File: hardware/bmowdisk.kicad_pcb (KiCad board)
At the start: 2 copper layers, 100 x 77.7 mm, 41 parts, among them CON1 IDC20, J1 MA06-1NORMAL, J2 MA04-1S, J3 LCD1, J4 M02PTH, U1 LCMXO2-1200HC-TQFP100, U2 SPI-FLASH, U3 MIC5219XX, U4 74X245, U5 74X245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

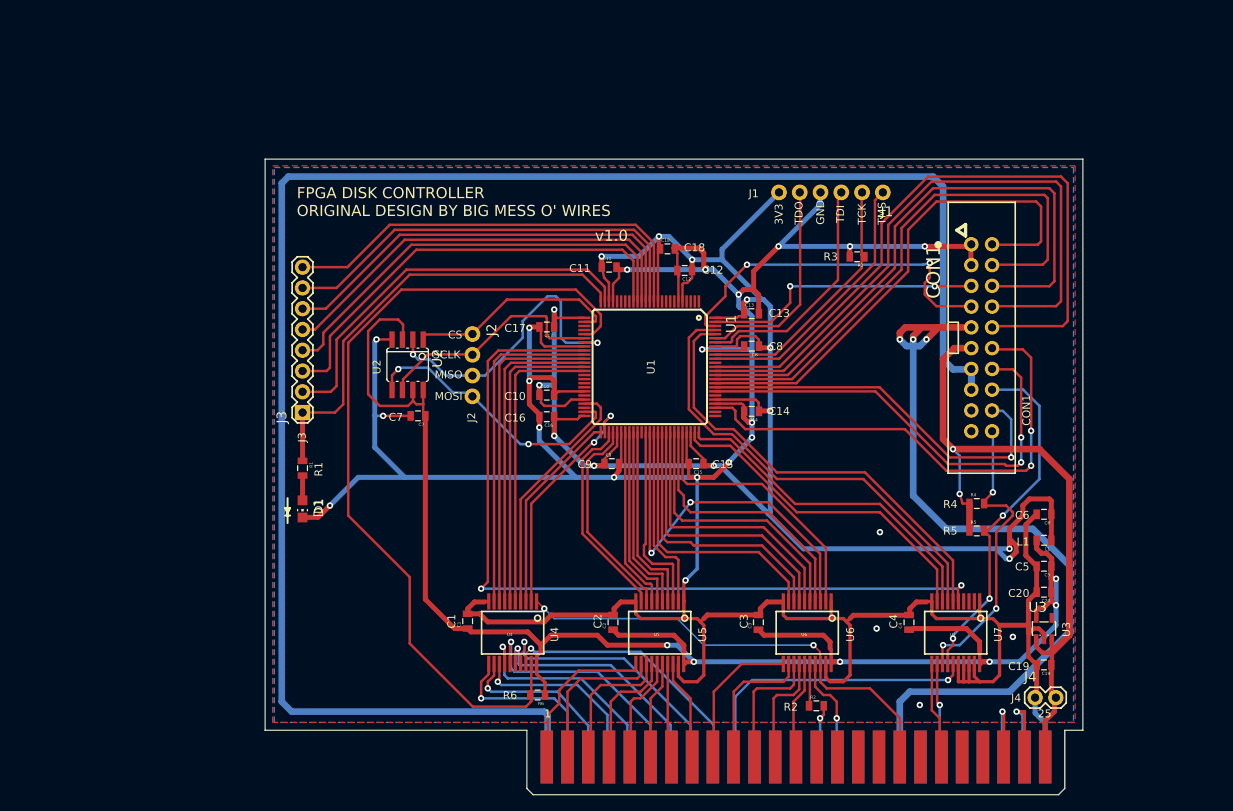
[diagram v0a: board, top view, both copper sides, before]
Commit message: Tidy up schematics, remove machxo2 FPGA and related components
Initial prototype version with headers for connecting olimex ice40-hx8k
fpga dev board for replacing the fpga

Signed-off-by: Rangel Ivanov <rangelivanov88@gmail.com>
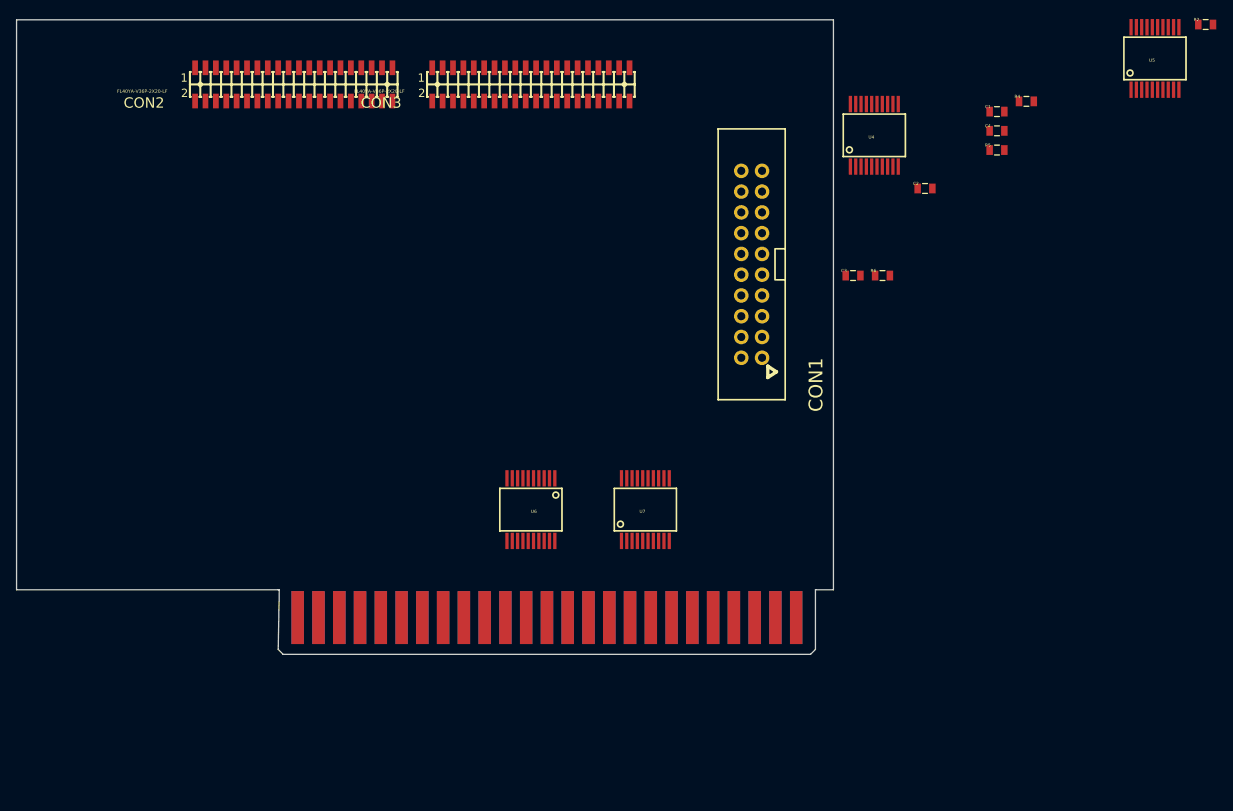
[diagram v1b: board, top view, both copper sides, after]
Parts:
- removed C10, C11, C12, C5, C6, C7, C8, C9: 0.1uF, bmowdisk:0805
- removed C13, C14, C15, C16, C17, C18: 0.01uF, bmowdisk:0805
- removed C19, C20: 10uF, bmowdisk:0805
- removed D1: LEDCHIP-LED0805, bmowdisk:CHIP-LED0805
- removed J1: MA06-1NORMAL, bmowdisk:MA06-1
- removed J2: MA04-1S, bmowdisk:MA04-1
- removed J3: LCD1, bmowdisk:1X08
- removed J4: M02PTH, bmowdisk:1X02
- removed L1: INDUCTOR0805, bmowdisk:0805
- removed R1: 390R, bmowdisk:0805
- removed R3: 4.7K, bmowdisk:0805
- removed U1: LCMXO2-1200HC-TQFP100, bmowdisk:TQFP100
- removed U2: SPI-FLASH, bmowdisk:SOIC08
- removed U3: MIC5219XX, bmowdisk:SOT23-5
- added CON2: FL40YA-V36P-2X20-LF, lime2-ice40-shield:YA-V36P-2X20-LF, F.Cu at (102.0, 57.0)
- added CON3: FL40YA-V36P-2X20-LF, lime2-ice40-shield:YA-V36P-2X20-LF, F.Cu at (131.0, 57.0)
- moved R2 96.0 mm to (213.5, 49.7)
- moved U5 92.7 mm to (207.3, 53.8), turned to 0 degrees
- moved C1 89.9 mm to (188.0, 60.3), turned to 0 degrees
- moved U4 75.2 mm to (173.0, 63.2), turned to 0 degrees
- moved R6 66.4 mm to (174.0, 80.4), turned to 0 degrees
- moved C2 65.4 mm to (179.2, 69.7), turned to 0 degrees
- moved C4 61.1 mm to (188.0, 62.7), turned to 0 degrees
- moved R4 49.6 mm to (191.6, 59.1)
- moved R5 46.6 mm to (188.0, 65.0)
- moved C3 44.0 mm to (170.4, 80.4), turned to 0 degrees
- moved U7 40.8 mm to (145.0, 109.0), turned to 0 degrees
- moved U6 37.0 mm to (131.0, 109.0)
- moved ST1 34.9 mm to (75.1, 92.4)
- moved CON1 29.5 mm to (158.0, 79.0), turned to 90 degrees
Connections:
- C1 pad 1: VCC -> /5V
- C2 pad 1: VCC -> /5V
- C3 pad 1: VCC -> /5V
- C4 pad 1: VCC -> /5V
- R6 pad 1: VCC -> /5V
- U4 pad 20: VCC -> /5V
- U5 pad 20: VCC -> /5V
- U6 pad 20: VCC -> /5V
- U7 pad 20: VCC -> /5V
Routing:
- net GND: track 437.4 -> 0.00 mm, vias 23 -> 0
- net /VCC_F: track 238.2 -> 0.00 mm, vias 13 -> 0
- net /12V: track 213.9 -> 0.00 mm
- net VCC: track 200.4 -> 0.00 mm, vias 6 -> 0
- net /EN245: track 102.3 -> 0.00 mm
- net //DEVSEL_33: track 101.6 -> 0.00 mm, vias 2 -> 0
- net /-12V: track 98.3 -> 0.00 mm, vias 3 -> 0
- net /5V: track 82.9 -> 0.00 mm, vias 2 -> 0
- net //WREQ: track 82.5 -> 0.00 mm
- net /PH3: track 77.8 -> 0.00 mm
- net /PH2: track 72.8 -> 0.00 mm
- net /PH1: track 67.7 -> 0.00 mm
- net /PH0: track 62.7 -> 0.00 mm
- net /SEL: track 61.1 -> 0.00 mm, vias 2 -> 0
- net /RW: track 57.2 -> 0.00 mm, vias 2 -> 0
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- removed copper zone on B.Cu, net GND
- removed copper zone on F.Cu, net GND
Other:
- board size 100 x 77.7 mm -> 99.9 x 77.6 mm
- board text removed: "1"
- board text removed: "25"
- board text removed: "3V3"
- board text removed: "C1"
- board text removed: "C10"
- board text removed: "C11"
- board text removed: "C12"
- board text removed: "C13"
- board text removed: "C14"
- board text removed: "C15"
- board text removed: "C16"
- board text removed: "C17"
- board text removed: "C18"
- board text removed: "C19"
- board text removed: "C2"
- board text removed: "C20"
- board text removed: "C3"
- board text removed: "C4"
- board text removed: "C5"
- board text removed: "C6"
- board text removed: "C7"
- board text removed: "C8"
- board text removed: "C9"
- board text removed: "CON1"
- board text removed: "CS"
- board text removed: "D1"
- board text removed: "FPGA DISK CONTROLLER ORIGINAL DESIGN BY BIG MESS O' WIRES"
- board text removed: "GND"
- board text removed: "J1"
- board text removed: "J2"
- board text removed: "J3"
- board text removed: "J4"
- board text removed: "L1"
- board text removed: "MISO"
- board text removed: "MOSI"
- board text removed: "R1"
- board text removed: "R2"
- board text removed: "R3"
- board text removed: "R4"
- board text removed: "R5"
- board text removed: "R6"
- board text removed: "SCLK"
- board text removed: "TCK"
- board text removed: "TDI"
- board text removed: "TDO"
- board text removed: "TMS"
- board text removed: "U1"
- board text removed: "U2"
- board text removed: "U3"
- board text removed: "U4"
- board text removed: "U5"
- board text removed: "U6"
- board text removed: "U7"
- board text removed: "v1.0"

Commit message: Place and route board
Signed-off-by: Rangel Ivanov <rangelivanov88@gmail.com>
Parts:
- removed CON1: IDC20, bmowdisk:IDC20
- removed CON2, CON3: FL40YA-V36P-2X20-LF, lime2-ice40-shield:YA-V36P-2X20-LF
- removed U5, U6, U7: 74X245, bmowdisk:SSOP20
- added C5: 0.1uF, bmowdisk:C_0805_2012Metric_Pad1.18x1.45mm_HandSolder, F.Cu at (164.9, 112.9)
- added C6: 0.1uF, bmowdisk:C_0805_2012Metric_Pad1.18x1.45mm_HandSolder, F.Cu at (136.7, 113.1)
- added C7: 0.1uF, bmowdisk:C_0805_2012Metric_Pad1.18x1.45mm_HandSolder, F.Cu at (120.5, 113.1)
- added C8: 0.1uF, bmowdisk:C_0805_2012Metric_Pad1.18x1.45mm_HandSolder, B.Cu at (105.4, 113.1)
- added R1: 2K2, bmowdisk:R_0805_2012Metric_Pad1.20x1.40mm_HandSolder, B.Cu at (123.3, 117.2)
- added R3: 3K3, bmowdisk:R_0805_2012Metric_Pad1.20x1.40mm_HandSolder, B.Cu at (123.3, 113.1)
- added TO DISK DRIVE: IDC20, bmowdisk:IDC20, F.Cu at (152.7, 99.8)
- added TO FPGA BOARD: FL40YA-V36P-2X20-LF, lime2-ice40-shield:YA-V36P-2X20-LF, F.Cu at (154.2, 86.1)
- added TO FPGA BOARD: FL40YA-V36P-2X20-LF, lime2-ice40-shield:YA-V36P-2X20-LF, F.Cu at (122.4, 86.1)
- added U1: SN74LVC8T245PW, kicad:TSSOP-24_4.4x7.8mm_P0.65mm, F.Cu at (158.3, 110.1)
- added U2: SN74LVC8T245PW, kicad:TSSOP-24_4.4x7.8mm_P0.65mm, F.Cu at (129.7, 110.1)
- added U3: SN74LVC8T245PW, kicad:TSSOP-24_4.4x7.8mm_P0.65mm, F.Cu at (114.9, 110.1)
- C1, C2, C3: footprint bmowdisk:0805 -> bmowdisk:C_0805_2012Metric_Pad1.18x1.45mm_HandSolder
- C4: footprint bmowdisk:0805 -> bmowdisk:C_0805_2012Metric_Pad1.18x1.45mm_HandSolder; moved to B.Cu
- R2, R5, R6: footprint bmowdisk:0805 -> bmowdisk:R_0805_2012Metric_Pad1.20x1.40mm_HandSolder
- R4: footprint bmowdisk:0805 -> bmowdisk:R_0805_2012Metric_Pad1.20x1.40mm_HandSolder; moved to B.Cu
- U4: value 74X245 -> SN74LVC8T245PW; footprint bmowdisk:SSOP20 -> kicad:TSSOP-24_4.4x7.8mm_P0.65mm; moved to B.Cu
- moved R2 102.4 mm to (137.0, 117.7)
- moved R4 96.9 mm to (109.3, 110.3), turned to 270 degrees
- moved C4 80.9 mm to (120.5, 107.3), turned to 270 degrees
- moved U4 74.6 mm to (114.9, 110.1), turned to 270 degrees
- moved C3 56.7 mm to (120.5, 107.3), turned to 270 degrees
- moved C2 56.7 mm to (136.7, 107.3), turned to 270 degrees
- moved C1 52.3 mm to (164.9, 107.3), turned to 270 degrees
- moved R5 49.2 mm to (168.2, 110.1), turned to 270 degrees
- moved R6 34.3 mm to (168.2, 114.1), turned to 270 degrees
- moved ST1 3.54 mm to (77.7, 94.7)
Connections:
- C1 pad 1: /5V -> /3.3V
- C2 pad 1: /5V -> /3.3V
- C3 pad 1: /5V -> /3.3V
- C4 pad 1: /5V -> /3.3V
- R4 pad 1: /5V -> /3.3V
- R4 pad 2: /SENSE -> /EN245
- R6 pad 2: /EN245 -> /SENSE
- ST1 pad 01: //IOSELECT -> /~IOSELECT
- ST1 pad 20: //IOSTROBE -> /~IOSTROBE
- ST1 pad 31: //RESET -> /~RESET
- U4 pad 1: /RW -> /3.3V
- U4 pad 10: GND -> /D7_33
- U4 pad 11: /D0 -> GND
- U4 pad 12: /D1 -> GND
- U4 pad 13: /D2 -> GND
- U4 pad 14: /D3 -> /D7
- U4 pad 15: /D4 -> /D6
- U4 pad 17: /D6 -> /D4
- U4 pad 18: /D7 -> /D3
- U4 pad 19: /EN245 -> /D2
- U4 pad 2: /D7_33 -> Net-(R1-Pad2)
- U4 pad 20: /5V -> /D1
- U4 pad 3: /D6_33 -> /D0_33
- U4 pad 4: /D5_33 -> /D1_33
- U4 pad 5: /D4_33 -> /D2_33
- U4 pad 7: /D2_33 -> /D4_33
- U4 pad 8: /D1_33 -> /D5_33
- U4 pad 9: /D0_33 -> /D6_33
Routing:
- net /5V: track 0.00 -> 267.0 mm, vias 0 -> 10
- net /3.3V: track 0.00 -> 169.8 mm, vias 0 -> 4
- net /12V: track 0.00 -> 69.5 mm, vias 0 -> 2
- net //DEVSEL: track 0.00 -> 37.4 mm, vias 0 -> 1
- net /RDDATA: track 0.00 -> 37.2 mm, vias 0 -> 2
- net /RW: track 0.00 -> 36.1 mm, vias 0 -> 1
- net /EN245: track 0.00 -> 36.0 mm, vias 0 -> 1
- net /SENSE: track 0.00 -> 30.1 mm, vias 0 -> 1
- net GND: track 0.00 -> 28.7 mm, vias 0 -> 59
- net /D7_33: track 0.00 -> 25.6 mm, vias 0 -> 1
- net /~DEVSEL_33: track 0.00 -> 25.6 mm
- net /D6_33: track 0.00 -> 25.4 mm, vias 0 -> 1
- net /D5_33: track 0.00 -> 25.1 mm, vias 0 -> 1
- net /D4_33: track 0.00 -> 24.9 mm, vias 0 -> 1
- net /-12V: track 0.00 -> 24.8 mm, vias 0 -> 2
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- added copper zone on B.Cu, net GND
- added copper zone on F.Cu, net GND
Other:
- board size 99.9 x 77.6 mm -> 68 x 47.7 mm
- board text added: "APPLE II Liron Card Clone"

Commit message: Fix connections to 0.05 inch headers
Signed-off-by: Rangel Ivanov <rangelivanov88@gmail.com>
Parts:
- CON1: renamed from TO DISK DRIVE
- CON2, CON3: renamed from TO FPGA BOARD
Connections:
- CON2 pad 10: /A0_33 -> /EN245
- CON2 pad 12: /A1_33 -> /~IOSELECT_33
- CON2 pad 14: /A2_33 -> /A0_33
- CON2 pad 16: /A3_33 -> /A1_33
- CON2 pad 18: /A4_33 -> /A2_33
- CON2 pad 20: /A5_33 -> /A3_33
- CON2 pad 22: /A6_33 -> /A4_33
- CON2 pad 24: /A7_33 -> /A5_33
- CON2 pad 26: /A8_33 -> /A6_33
- CON2 pad 28: /A9_33 -> /A7_33
- CON2 pad 30: /A10_33 -> /A8_33
- CON2 pad 32: /A11_33 -> /A9_33
- CON2 pad 34: Net-(CON2-Pad34) -> /A10_33
- CON2 pad 36: /Q3R_33 -> /A11_33
- CON2 pad 38: /7M_33 -> /Q3R_33
- CON2 pad 39: Net-(CON2-Pad39) -> /RW_33
- CON2 pad 40: /RW_33 -> /7M_33
- CON2 pad 6: /EN245 -> Net-(CON2-Pad6)
- CON2 pad 8: /~IOSELECT_33 -> Net-(CON2-Pad8)
- CON3 pad 10: /PH2 -> /PH0
- CON3 pad 12: /PH3 -> /PH1
- CON3 pad 14: /~WREQ -> /PH2
- CON3 pad 16: /SEL -> /PH3
- CON3 pad 18: /~ENABLE1 -> /~WREQ
- CON3 pad 20: /WRDATA -> /SEL
- CON3 pad 22: /~IOSTROBE_33 -> /~ENABLE1
- CON3 pad 24: /~RESET_33 -> /WRDATA
- CON3 pad 26: /SENSE_33 -> /~IOSTROBE_33
- CON3 pad 28: /RDDATA_33 -> /~RESET_33
- CON3 pad 30: /~DEVSEL_33 -> /SENSE_33
- CON3 pad 32: Net-(CON3-Pad32) -> /RDDATA_33
- CON3 pad 34: Net-(CON3-Pad34) -> /~DEVSEL_33
- CON3 pad 6: /PH0 -> Net-(CON3-Pad6)
- CON3 pad 8: /PH1 -> Net-(CON3-Pad8)
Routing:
- net GND: track 28.7 -> 23.0 mm, vias 59 -> 62
- net /RW_33: track 20.2 -> 24.8 mm
- net /WRDATA: track 15.5 -> 12.7 mm
- net /Q3R_33: track 19.7 -> 22.3 mm
- net /SENSE_33: track 21.5 -> 23.8 mm
- net /RDDATA_33: track 23.6 -> 25.7 mm
- net /A6_33: track 21.6 -> 23.3 mm
- net /A5_33: track 21.3 -> 23.1 mm
- net /A11_33: track 19.4 -> 21.1 mm
- net /A4_33: track 21.1 -> 22.5 mm
- net /EN245: track 36.0 -> 37.2 mm
- net /~ENABLE1: track 12.2 -> 11.1 mm, vias 1 -> 0
- net /A2_33: track 20.5 -> 21.6 mm
- net /A1_33: track 20.3 -> 21.3 mm
- net /A0_33: track 20.0 -> 21.1 mm
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
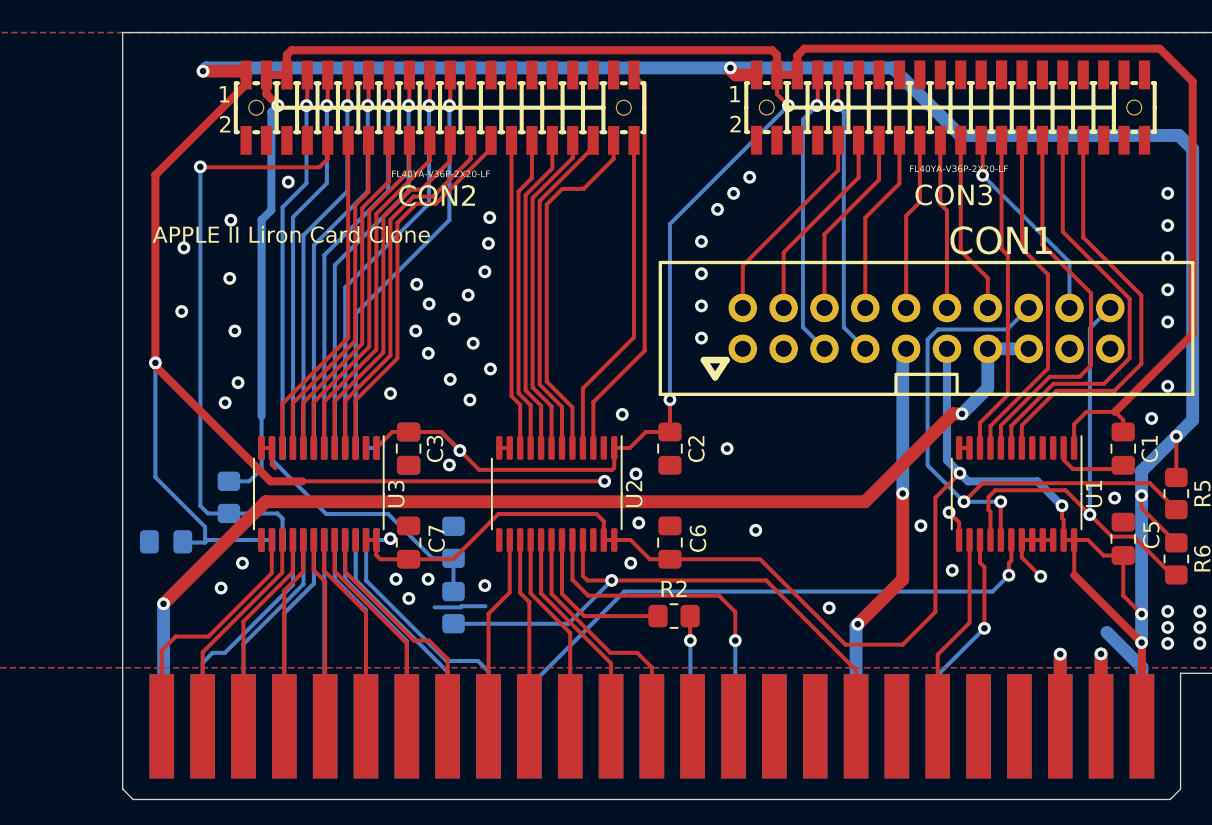
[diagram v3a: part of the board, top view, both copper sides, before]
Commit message: Remove silk screen from 0.5" headers
Add text for connections to FPGA board

Signed-off-by: Rangel Ivanov <rangelivanov88@gmail.com>
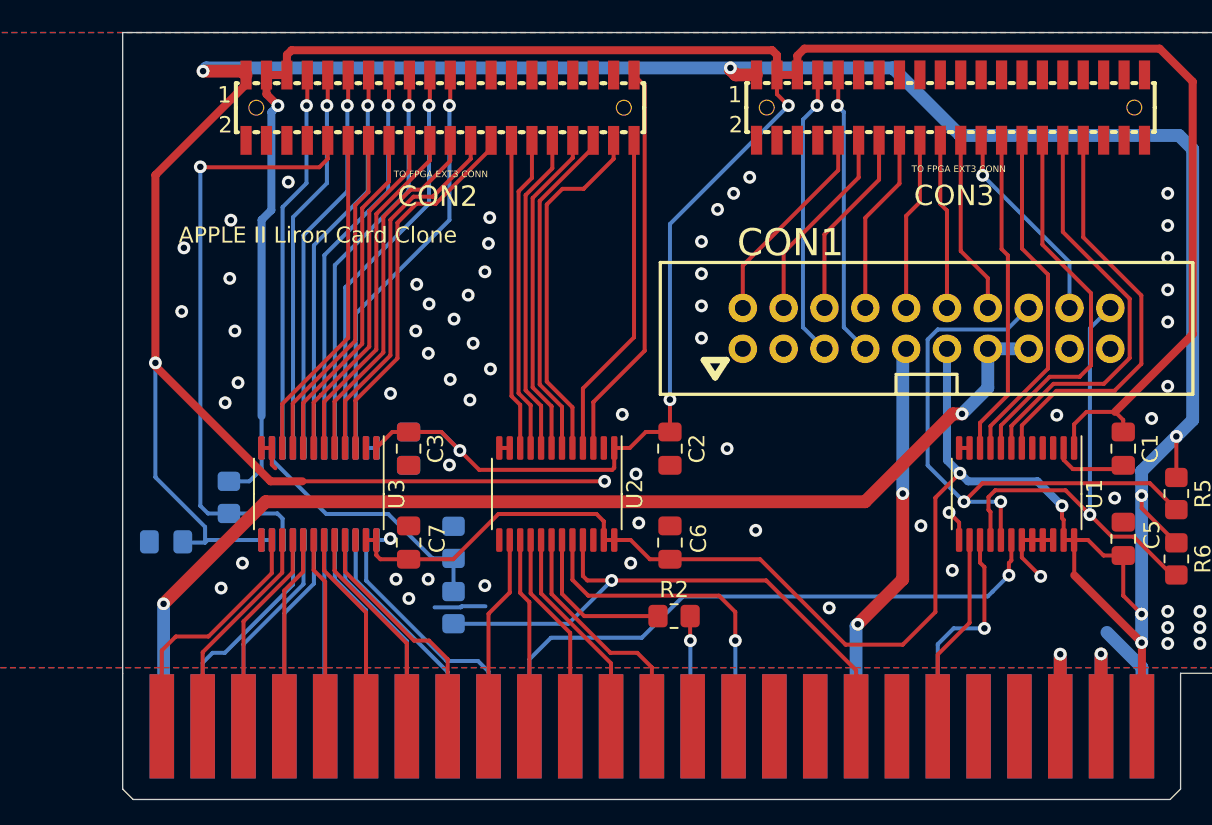
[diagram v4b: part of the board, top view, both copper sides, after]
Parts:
- CON1: value IDC20 -> TO DISK DRIVE
- CON2, CON3: value FL40YA-V36P-2X20-LF -> TO FPGA EXT3 CONN
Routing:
- net /~RESET: track 12.9 -> 17.2 mm
- net //DEVSEL: track 37.4 -> 40.9 mm
- net GND: vias 62 -> 63

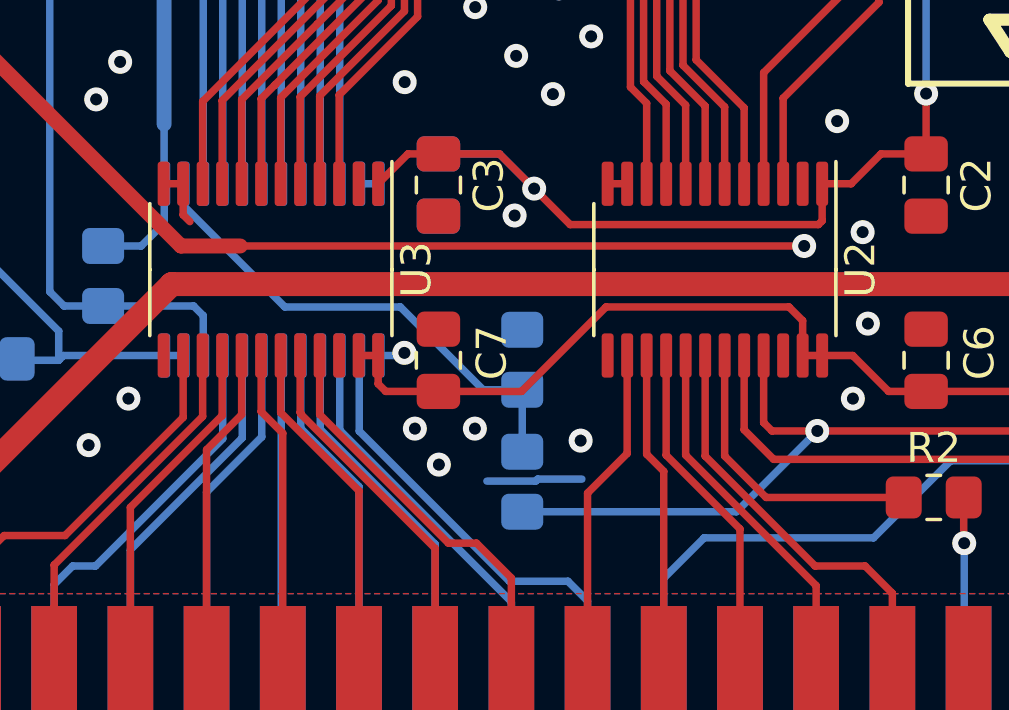
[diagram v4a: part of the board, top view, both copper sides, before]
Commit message: Remove voltage divider for RW line to bus transceiver
Signed-off-by: Rangel Ivanov <rangelivanov88@gmail.com>
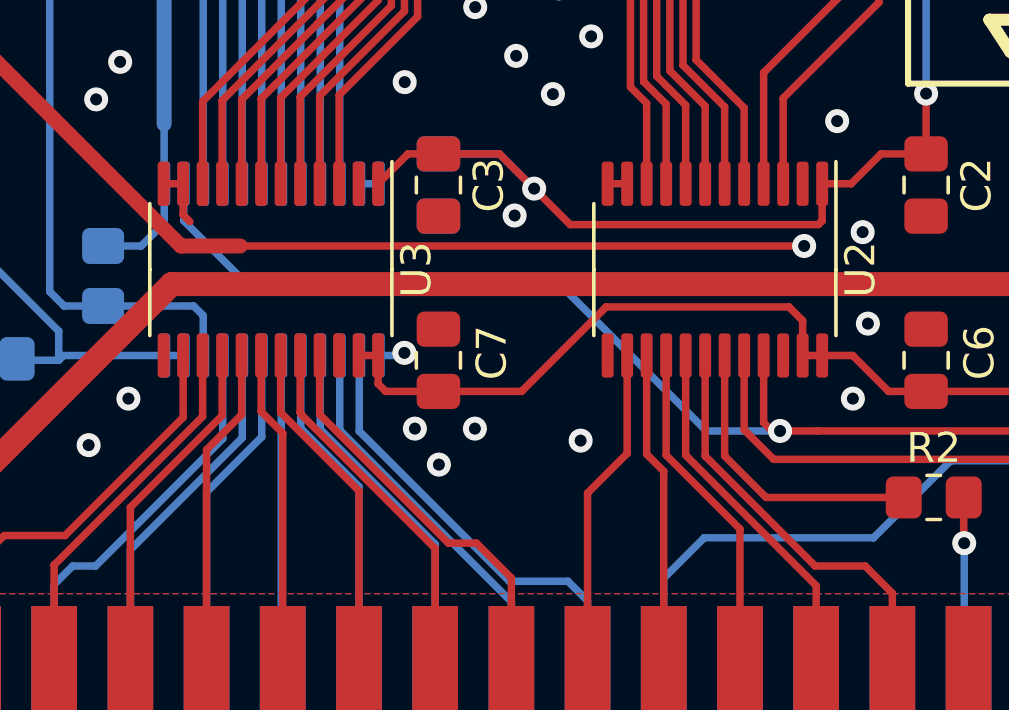
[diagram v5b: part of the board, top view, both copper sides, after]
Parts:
- removed R1: 2K2, bmowdisk:R_0805_2012Metric_Pad1.20x1.40mm_HandSolder
- removed R3: 3K3, bmowdisk:R_0805_2012Metric_Pad1.20x1.40mm_HandSolder
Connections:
- U4 pad 2: Net-(R1-Pad2) -> /RW
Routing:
- net Net-(R1-Pad2): track 16.6 -> 0.00 mm
- net /RW: track 36.1 -> 49.2 mm
- net (no net): track 3.19 -> 0.00 mm
